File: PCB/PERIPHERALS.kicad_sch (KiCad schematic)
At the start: 0 parts

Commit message: Agregado RS485, Smart Switch, ORING Diode
Se termino de acabar todo el esquematico, solo falta crear el footprint para un inductor
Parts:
- added C300: 1uF, Capacitor_SMD:C_0603_1608Metric_Pad1.08x0.95mm_HandSolder, symbol Device:C_Small
- added C301: 0.1uF, Capacitor_SMD:C_0603_1608Metric, symbol Device:C_Small
- added D300: PMEG3030EP,115, Diode_SMD:D_SOD-128, symbol Diode:PMEG4050EP
- added D301: LED_DOOR, LED_SMD:LED_0603_1608Metric, symbol Device:LED
- added D302: SMAJ15A, Diode_SMD:D_SMA, symbol Diode:SMAJ15A
- added D303, D304: SMAJ30CA, Diode_SMD:D_SMA, symbol Diode:SMAJ30CA
- added J300: 2604-3102, 2604-3102:2604-3102, symbol 2604-3102:2604-3102
- added J301: jumper, Connector_PinHeader_2.54mm:PinHeader_1x02_P2.54mm_Vertical, symbol Connector:Conn_01x02_Pin
- added J302, J303: 2086-1104, 2086-1104-THT:2086-1104-THT, symbol 2086-1104-THT:2086-1104
- added R1, R2, R3, R303, R306, R307, R309, R4: 10K, Resistor_SMD:R_0603_1608Metric, symbol Device:R_Small
- added R300, R301, R302: 4.7k, Resistor_SMD:R_0603_1608Metric, symbol Device:R
- added R304: 2K, Resistor_SMD:R_0603_1608Metric, symbol Device:R
- added R305: 1k, Resistor_SMD:R_0603_1608Metric, symbol Device:R_Small
- added R308: 120, Resistor_SMD:R_0603_1608Metric, symbol Device:R_Small
- added S300: TPS1H200AQDGNRQ1, TPS1H200AQDGNRQ1:SOP65P490X110-9N, symbol TPS1H200AQDGNRQ1:TPS1H200AQDGNRQ1
- added SW300: SW_DIP_x05, DSIC-05-LS-GER:DSIC-05-LS-GER, symbol Switch:SW_DIP_x05
- added U300: THVD2450VDRCR, THVD2450VDRCR:VSON10_DRC_TEX, symbol THVD2450VDRCR:THVD2450VDRCR
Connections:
- new net: R304.2, S300.4 (CL)
- new net: D301.2 (A), R305.1
- new net: J301.1 (Pin_1), R308.1
- new net: R300.2, S300.1 (IN)
- new net: R301.2, S300.2 (DIAG_EN)
- new net: R302.2, R303.2, S300.3 (~{FAULT})
- new net: C300.2, S300.5 (DELAY)
- new net: D302.1 (A1), J300.3 (2_1), J300.4 (2_2), R305.2, S300.7 (OUT)
- new net: D300.1 (K), S300.8 (VS)
- new net +12V: D300.2 (A)
- new net +3.3V: C301.1, R303.1, R307.1, SW300.1, SW300.2, SW300.3, SW300.4, SW300.5, U300.1 (VIO), U300.10 (VCC), U300.7 (SLR)
- new net A: D303.2 (A2), J302.P4_1, J302.P4_2, J303.P1_1, J303.P1_2, R308.2, U300.8 (A)
- new net B: D304.2 (A2), J301.2 (Pin_2), J302.P3_1, J302.P3_2, J303.P2_1, J303.P2_2, U300.9 (B)
- new net DOOR_DIAG_EN: R301.1
- new net DOOR_EN: R300.1
- new net DOOR_FAULT: R302.1
- new net GND: C300.1, C301.2, D301.1 (K), D302.2 (A2), D303.1 (A1), D304.1 (A1), J300.1 (1_1), J300.2 (1_2), J302.P2_1, J302.P2_2, J303.P3_1, J303.P3_2, R1.1, R2.1, R3.1, R304.1, R306.2, R309.1, R4.1, S300.6 (GND), S300.9 (EP), U300.11 (GND), U300.6 (GND)
- new net ID1: R309.2, SW300.10
- new net ID2: R1.2, SW300.9
- new net ID3: R2.2, SW300.8
- new net ID4: R4.2, SW300.7
- new net ID5: R3.2, SW300.6
- new net RS485_EN: R306.1, U300.3 (DE), U300.4 (*RE)
- new net RX: R307.2, U300.2 (R)
- new net SHIELD: J302.P1_1, J302.P1_2, J303.P4_1, J303.P4_2
- new net TX: U300.5 (D)
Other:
- note added: "12V@200mA"
- note added: "ID SELECTOR"
- note added: "RELAY DRIVER FOR DOOR"
- note added: "RS485"
- note added: "RS485 CONNECTORS"
- note added: "[3] PERIPHERALS"

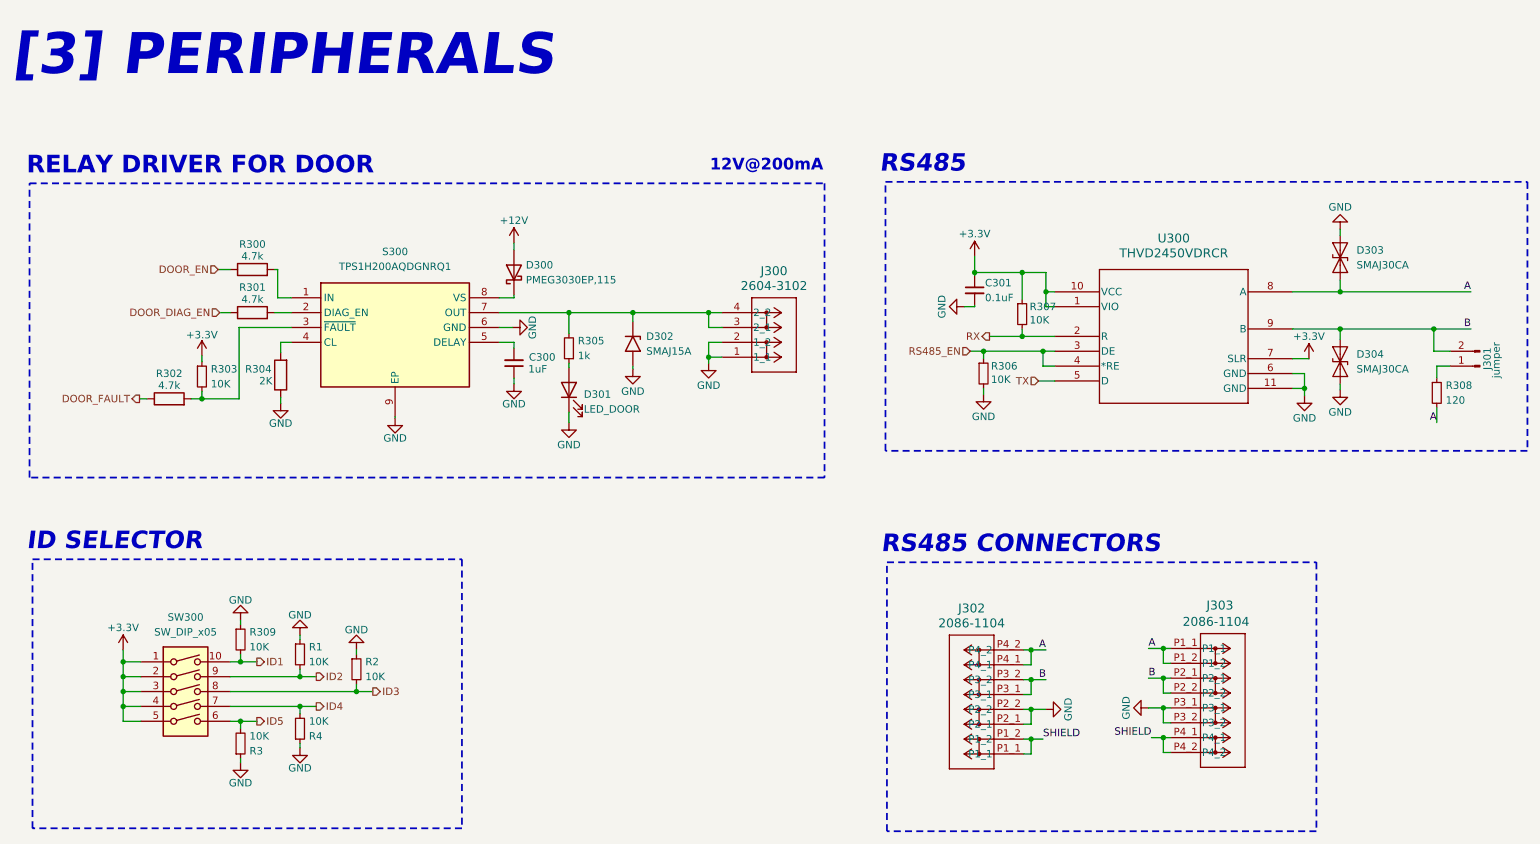
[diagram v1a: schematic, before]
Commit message: Placement
Se termino de crear el footprint para el inductor y placement en la PCB
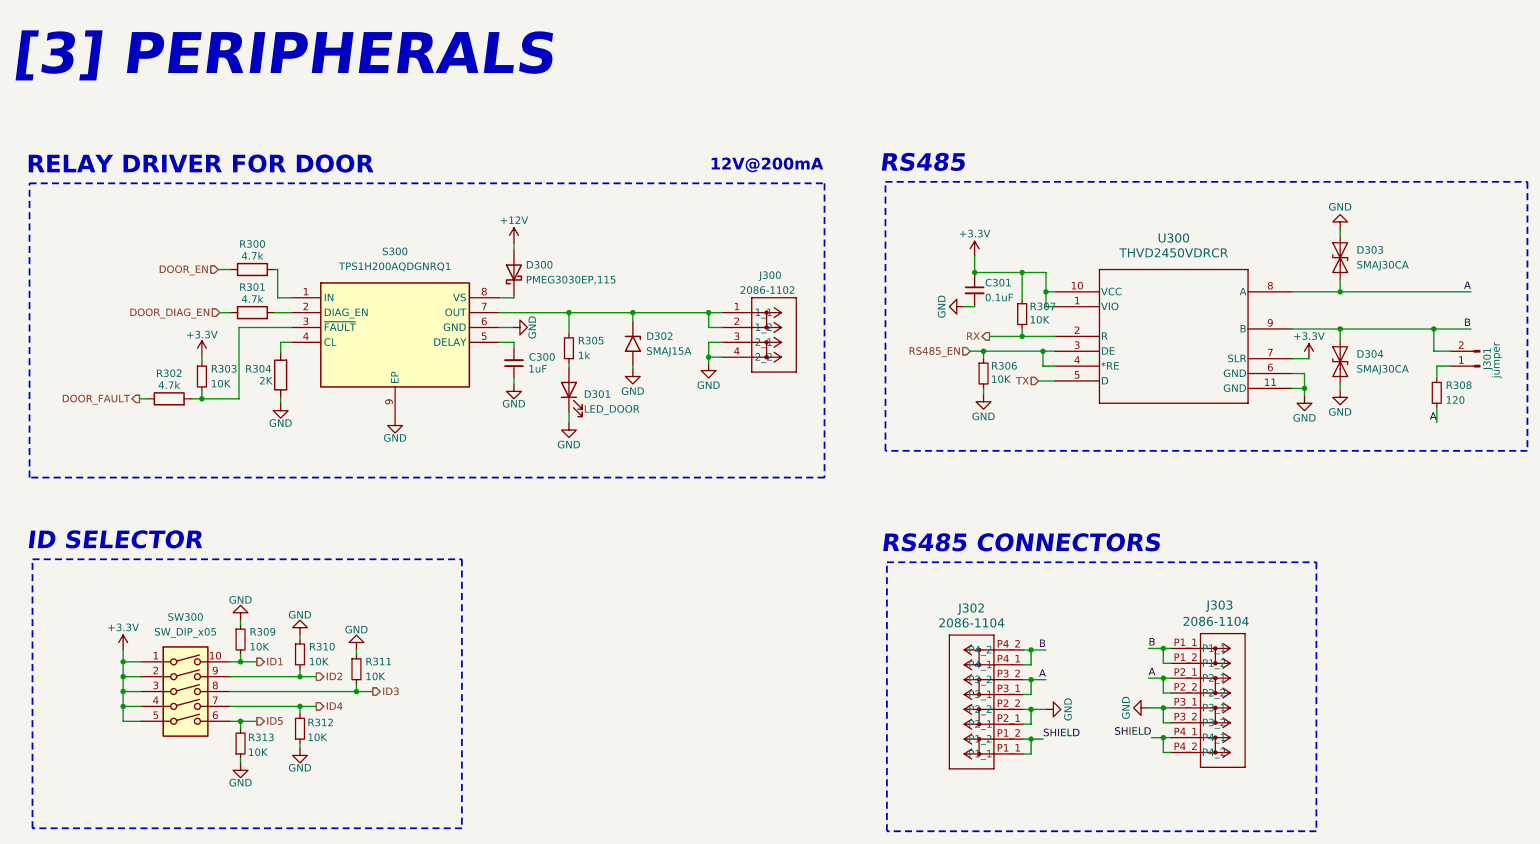
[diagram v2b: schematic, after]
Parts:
- removed J300: 2604-3102, 2604-3102:2604-3102, symbol 2604-3102:2604-3102
- added J300: 2086-1102, 2086-1102-THT:2086-1102-THT, symbol 2086-1102:2086-1102
- renumbered R1 to R310, R2 to R311, R4 to R312, R3 to R313
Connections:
- net A: now also J302.P3_1, J302.P3_2, J303.P2_1, J303.P2_2; no longer J302.P4_1, J302.P4_2, J303.P1_1, J303.P1_2
- net B: now also J302.P4_1, J302.P4_2, J303.P1_1, J303.P1_2; no longer J302.P3_1, J302.P3_2, J303.P2_1, J303.P2_2
- net GND: now also J300.3 (2_1), J300.4 (2_2)
- net at D302.1 (A1), R305.2, S300.7 (OUT): now also J300.1 (1_1), J300.2 (1_2)
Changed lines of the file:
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@@
 	)
 	(label "A"
-		(at 209.55 122.428 0)
+		(at 209.55 127.508 0)
 		(fields_autoplaced yes)
 		(effects
@@
 	)
 	(label "A"
-		(at 192.024 122.682 180)
+		(at 192.024 127.762 180)
 		(fields_autoplaced yes)
 		(effects
@@
 	)
 	(label "B"
-		(at 209.55 127.508 0)
+		(at 209.55 122.428 0)
 		(fields_autoplaced yes)
 		(effects
@@
 	)
 	(label "B"
-		(at 192.024 127.762 180)
+		(at 192.024 122.682 180)
 		(fields_autoplaced yes)
 		(effects
@@
 	)
 	(symbol
+		(lib_id "2086-1102:2086-1102")
+		(at 145.542 61.214 0)
+		(unit 1)
+		(exclude_from_sim no)
+		(in_bom yes)
+		(on_board yes)
+		(dnp no)
+		(property "Reference" "J300"
+			(at 143.002 58.674 0)
+			(effects
+				(font
+					(size 1.27 1.27)
+				)
+				(justify left)
+			)
+		)
+		(property "Value" "2086-1102"
+			(at 139.7 61.214 0)
+			(effects
+				(font
+					(size 1.27 1.27)
+				)
+				(justify left)
+			)
+		)
+		(property "Footprint" "2086-1102-THT:2086-1102-THT"
+			(at 145.542 61.214 0)
+			(effects
+				(font
+					(size 1.27 1.27)
+				)
+				(hide yes)
+			)
+		)
+		(property "Datasheet" ""
+			(at 145.542 61.214 0)
+			(effects
+				(font
+					(size 1.27 1.27)
+				)
+				(hide yes)
+			)
+		)
+		(property "Description" ""
+			(at 145.542 61.214 0)
+			(effects
+				(font
+					(size 1.27 1.27)
+				)
+				(hide yes)
+			)
+		)
+		(pin "3"
+		)
+		(pin "4"
+		)
+		(pin "1"
+		)
+		(pin "2"
+		)
+		(instances
+			(project ""
+				(path "/118ffa26-3c65-424a-af71-04338c4de0b0/f6cc8bac-4400-4ee5-8b53-8fb1b71d0580"
+					(reference "J300")
+					(unit 1)
+				)
+			)
+		)
+	)
+	(symbol
 		(lib_id "Device:R")
 		(at 61.214 75.692 180)
@@
 		(on_board yes)
 		(dnp no)
-		(property "Reference" "R3"
-			(at 55.88 139.954 0)
+		(property "Reference" "R313"
+			(at 55.626 137.668 0)
 			(effects
 				(font
@@
 		)
 		(property "Value" "10K"
-			(at 55.88 137.414 0)
+			(at 55.626 140.208 0)
 			(effects
 				(font
@@
 			(project "PCB-Cuarto"
 				(path "/118ffa26-3c65-424a-af71-04338c4de0b0/f6cc8bac-4400-4ee5-8b53-8fb1b71d0580"
-					(reference "R3")
+					(reference "R313")
 					(unit 1)
 				)
@@
 		(on_board yes)
 		(dnp no)
-		(property "Reference" "R2"
+		(property "Reference" "R311"
 			(at 75.692 124.714 0)
 			(effects
@@
 			(project "PCB-Cuarto"
 				(path "/118ffa26-3c65-424a-af71-04338c4de0b0/f6cc8bac-4400-4ee5-8b53-8fb1b71d0580"
-					(reference "R2")
-					(unit 1)
-				)
-			)
-		)
-	)
-	(symbol
-		(lib_id "2604-3102:2604-3102")
-		(at 136.652 72.644 0)
-		(mirror x)
-		(unit 1)
-		(exclude_from_sim no)
-		(in_bom yes)
-		(on_board yes)
-		(dnp no)
-		(property "Reference" "J300"
-			(at 145.542 57.912 0)
-			(effects
-				(font
-					(size 1.524 1.524)
-				)
-			)
-		)
-		(property "Value" "2604-3102"
-			(at 145.542 60.452 0)
-			(effects
-				(font
-					(size 1.524 1.524)
-				)
-			)
-		)
-		(property "Footprint" "2604-3102:2604-3102"
-			(at 136.652 72.644 0)
-			(effects
-				(font
-					(size 1.27 1.27)
-					(italic yes)
-				)
-				(hide yes)
-			)
-		)
-		(property "Datasheet" "2604-3102"
-			(at 136.652 72.644 0)
-			(effects
-				(font
-					(size 1.27 1.27)
-					(italic yes)
-				)
-				(hide yes)
-			)
-		)
-		(property "Description" ""
-			(at 136.652 72.644 0)
-			(effects
-				(font
-					(size 1.27 1.27)
-				)
-				(hide yes)
-			)
-		)
-		(pin "4"
-		)
-		(pin "3"
-		)
-		(pin "2"
-		)
-		(pin "1"
-		)
-		(instances
-			(project "PCB-Cuarto"
-				(path "/118ffa26-3c65-424a-af71-04338c4de0b0/f6cc8bac-4400-4ee5-8b53-8fb1b71d0580"
-					(reference "J300")
+					(reference "R311")
 					(unit 1)
 				)
@@
 		(on_board yes)
 		(dnp no)
-		(property "Reference" "R4"
-			(at 66.04 137.414 0)
+		(property "Reference" "R312"
+			(at 65.786 135.128 0)
 			(effects
 				(font
@@
 		)
 		(property "Value" "10K"
-			(at 66.04 134.874 0)
+			(at 65.786 137.668 0)
 			(effects
 				(font
@@
 			(project "PCB-Cuarto"
 				(path "/118ffa26-3c65-424a-af71-04338c4de0b0/f6cc8bac-4400-4ee5-8b53-8fb1b71d0580"
-					(reference "R4")
+					(reference "R312")
 					(unit 1)
 				)
@@
 		(on_board yes)
 		(dnp no)
-		(property "Reference" "R1"
+		(property "Reference" "R310"
 			(at 66.04 122.174 0)
 			(effects
@@
 			(project "PCB-Cuarto"
 				(path "/118ffa26-3c65-424a-af71-04338c4de0b0/f6cc8bac-4400-4ee5-8b53-8fb1b71d0580"
-					(reference "R1")
+					(reference "R310")
 					(unit 1)
 				)

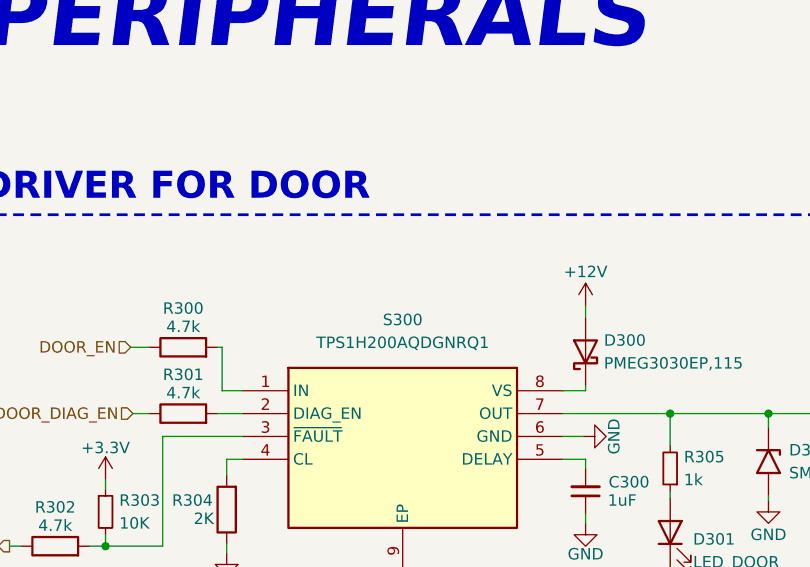
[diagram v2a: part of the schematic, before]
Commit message: Mejora en ruteo
- Se ha mejorado el ruteo de potencia
- Se ha generado los files para JLCPCB
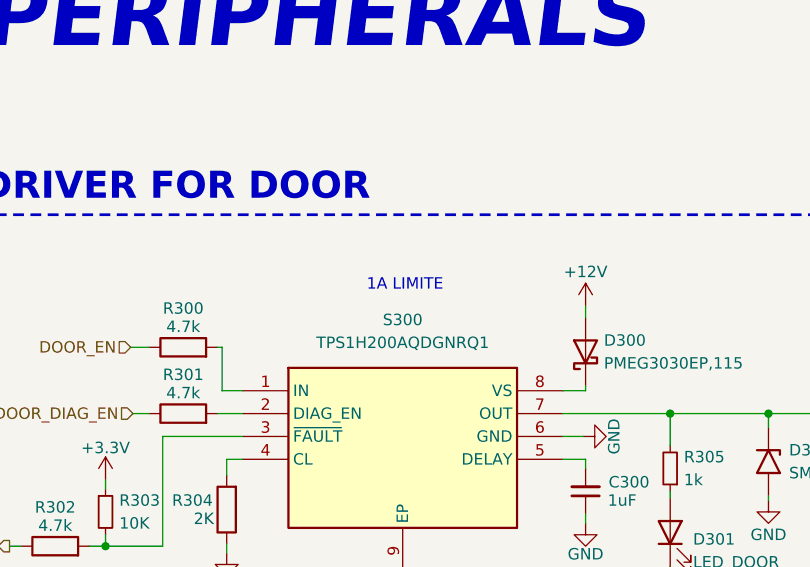
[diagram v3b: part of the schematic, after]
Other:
- note added: "1A LIMITE"
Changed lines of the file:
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@@
+		)
+	)
+	(text "1A LIMITE"
+		(exclude_from_sim no)
+		(at 81.026 50.8 0)
+		(effects
+			(font
+				(size 1.27 1.27)
+			)
 		)
 	)

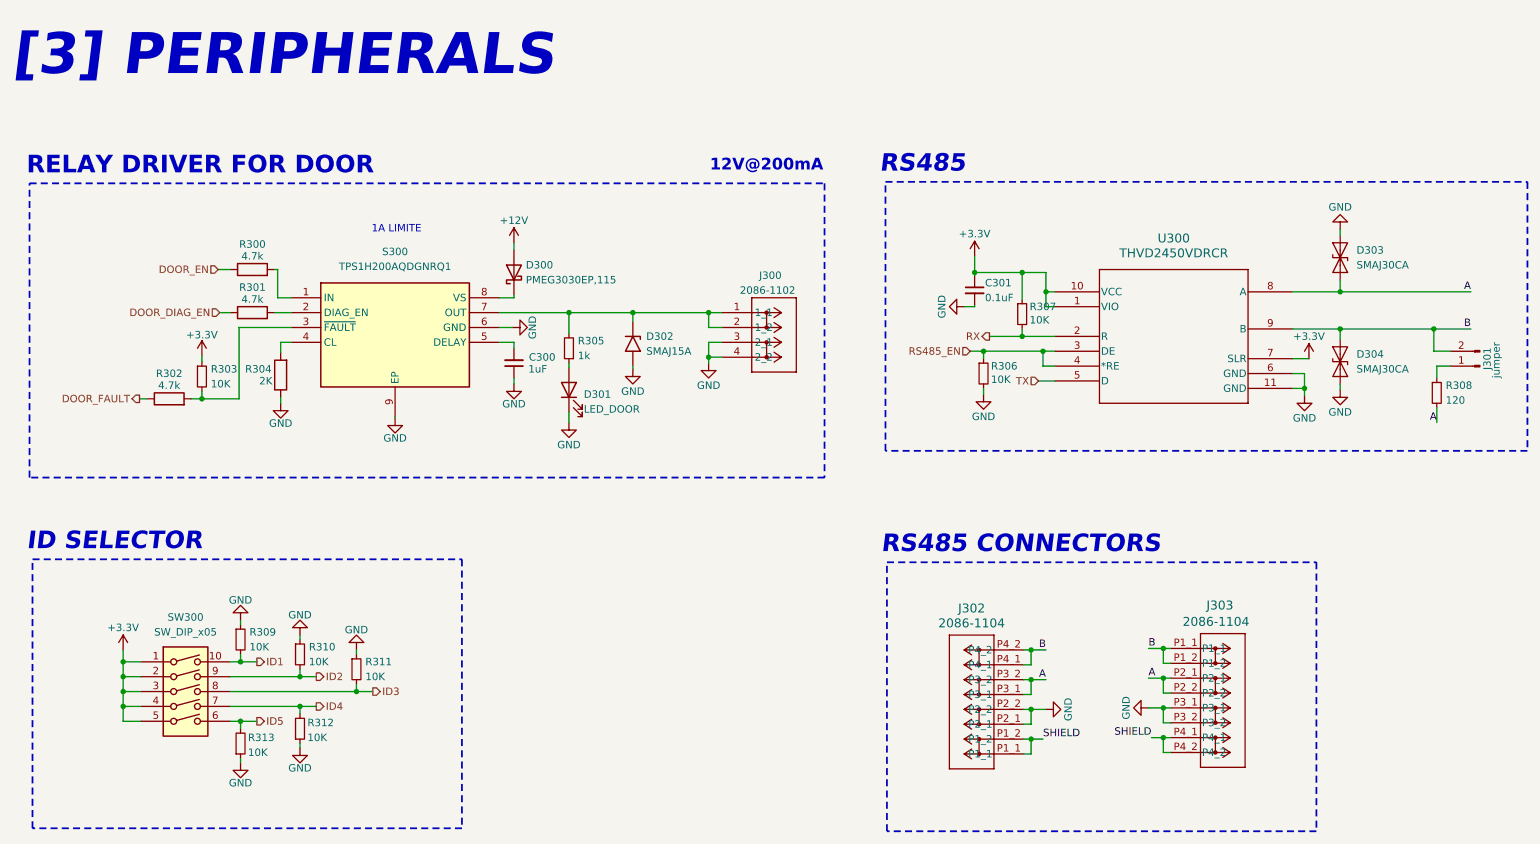
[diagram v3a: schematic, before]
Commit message: Change Placement
Se ha cambiado el placement total para obtener una mejor posicion de conexion de los perifericos
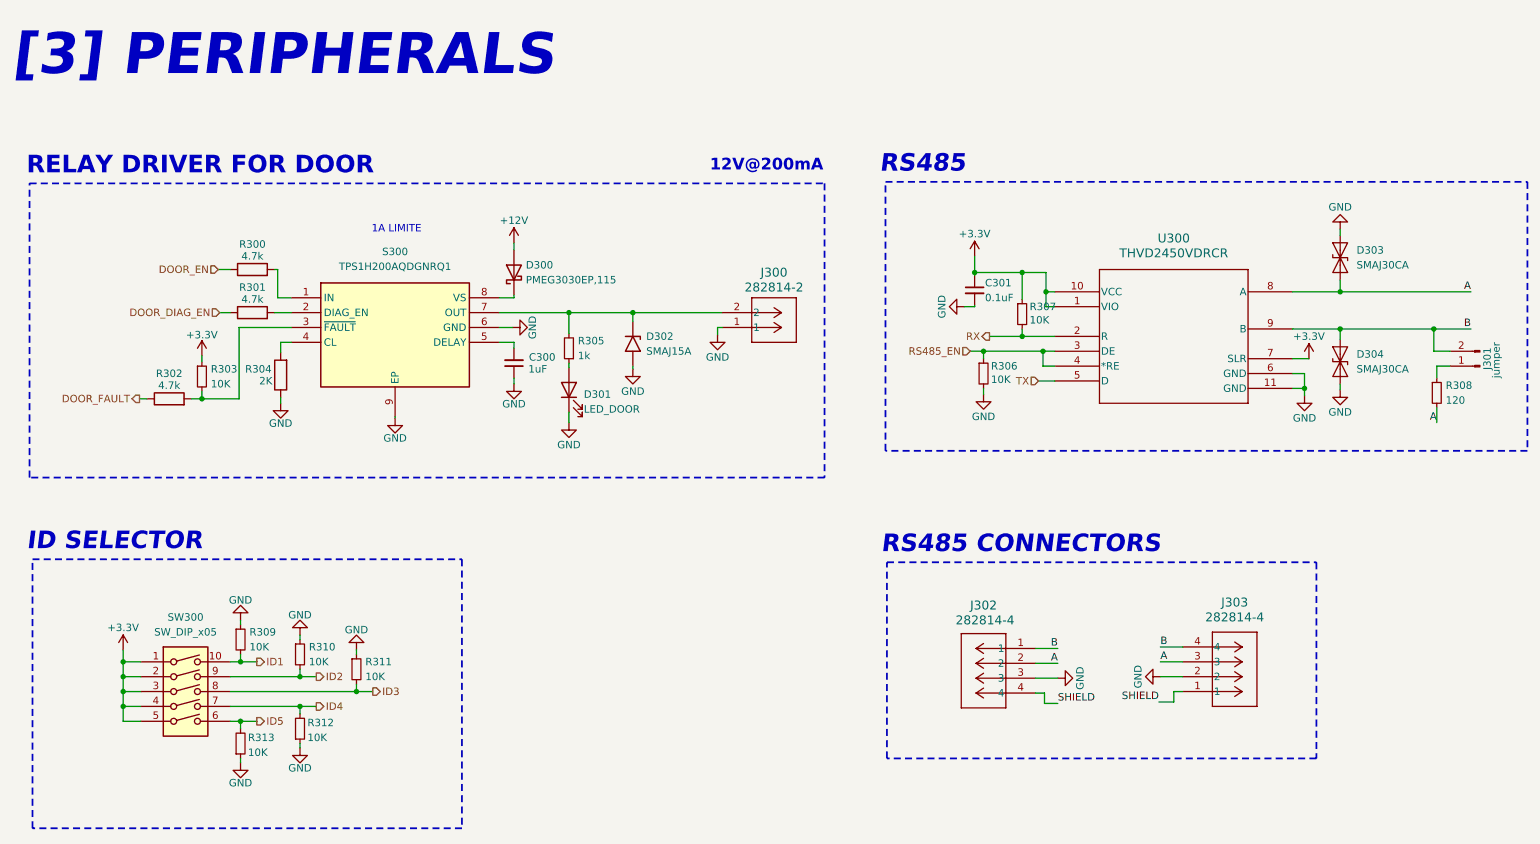
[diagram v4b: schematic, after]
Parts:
- removed J300: 2086-1102, 2086-1102-THT:2086-1102-THT, symbol 2086-1102:2086-1102
- removed J302, J303: 2086-1104, 2086-1104-THT:2086-1104-THT, symbol 2086-1104-THT:2086-1104
- added J300: 282814-2, 282814-2:282814-2, symbol 282814-2:282814-2
- added J302, J303: 282814-4, 282814-4:282814-4, symbol 282814-4:282814-4
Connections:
- net A: now also J302.2, J303.3
- net B: now also J302.1, J303.4
- net GND: now also J300.1, J302.3, J303.2
- net SHIELD: now also J302.4, J303.1
- net at D302.1 (A1), R305.2, S300.7 (OUT): now also J300.2
